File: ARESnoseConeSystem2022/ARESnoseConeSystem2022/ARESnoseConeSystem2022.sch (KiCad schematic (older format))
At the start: 15 parts, among them J1 436500200, J2 436500200, J3 BMP390_Headers, J4 ICM20948_Headers, J5 GPS_Headers1, J6 Transmitter_Headers1, J7 Conn_01x08, J8 Transmitter_Headers2, U1 BA05CC0WFP-E2, U2 Teensy4.1

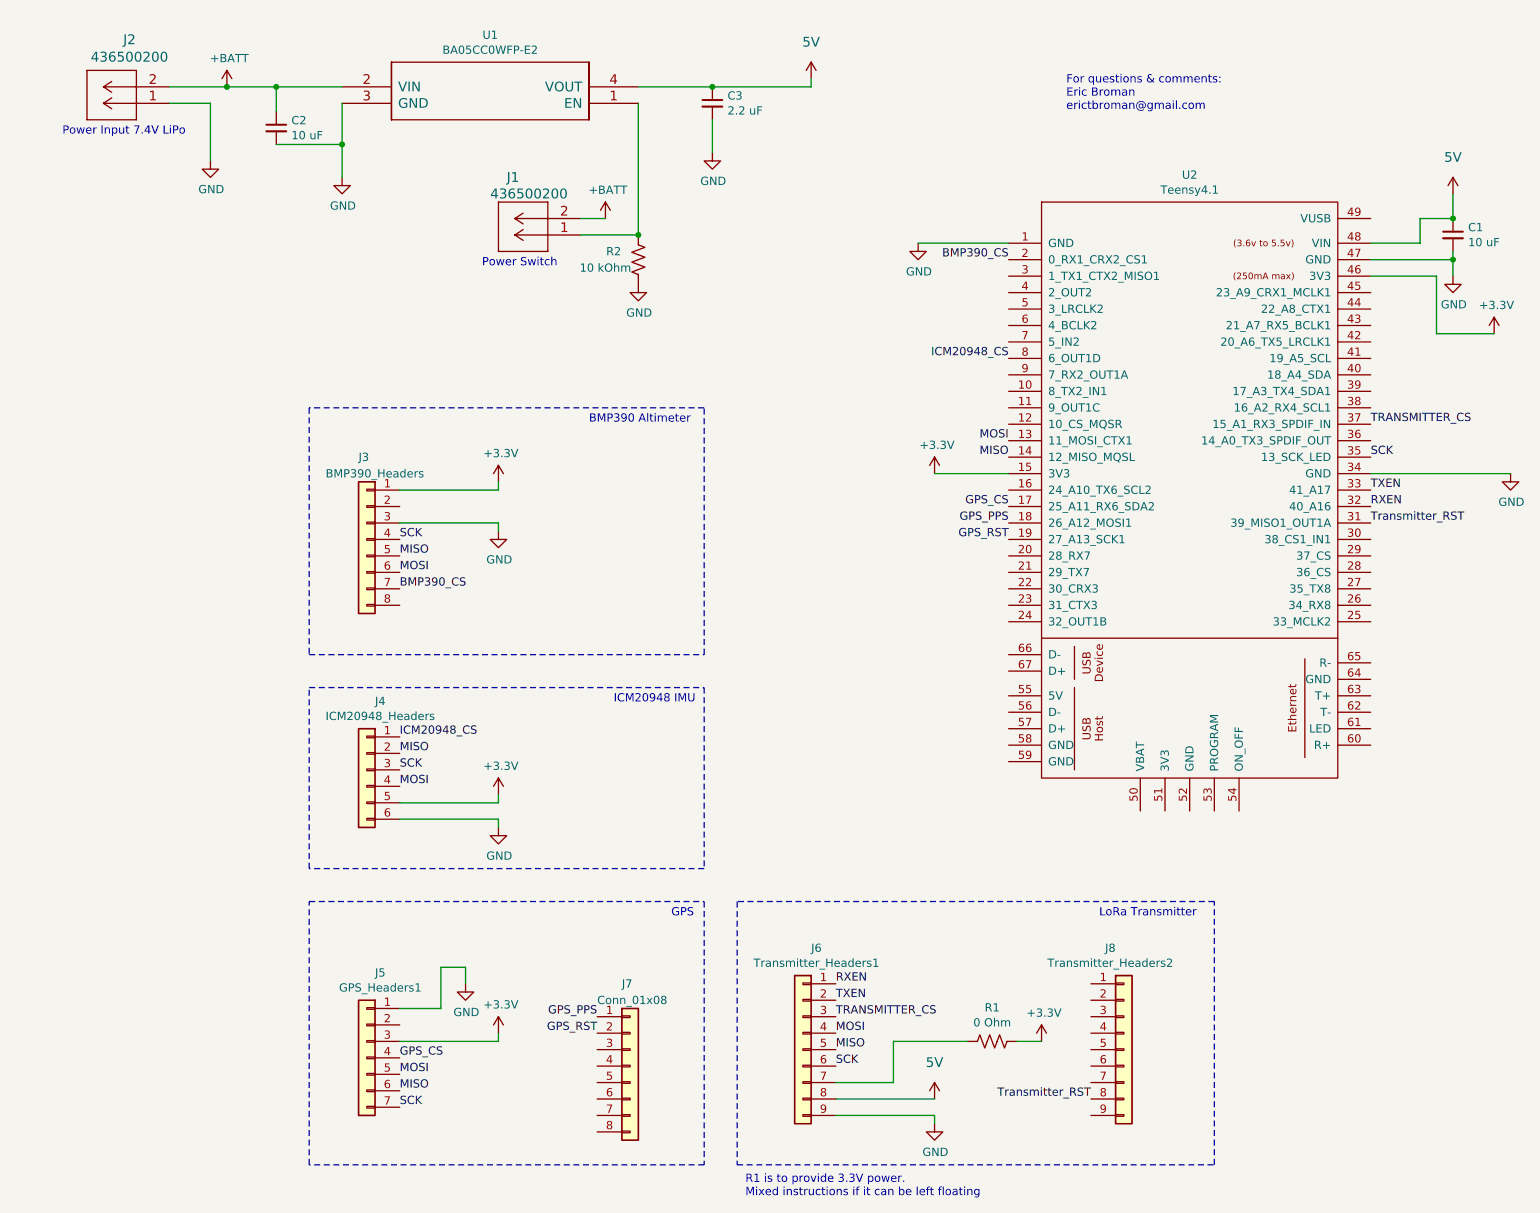
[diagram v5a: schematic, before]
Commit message: Finalized System V3
Added better radio board access and system power stabiity
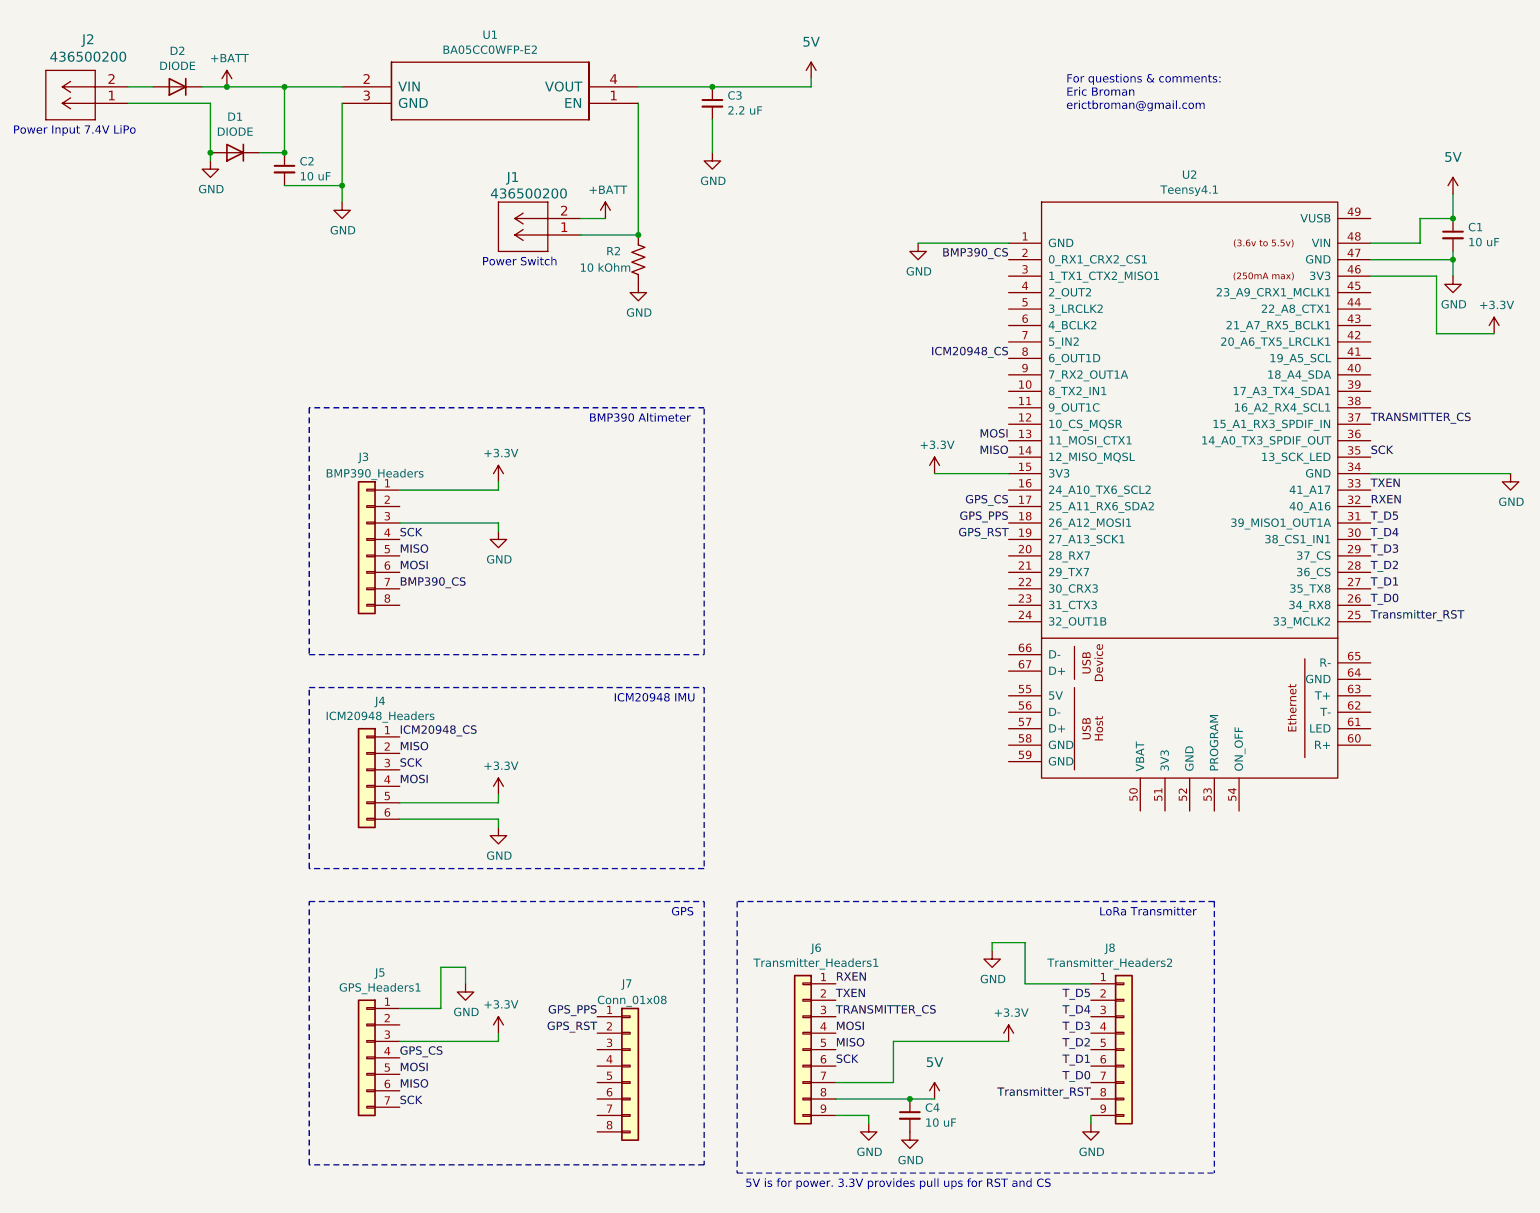
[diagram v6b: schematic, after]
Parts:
- removed R1: 0 Ohm, Resistor_SMD:R_0805_2012Metric_Pad1.15x1.40mm_HandSolder, symbol Device:R_US
- added C4: 10 uF, Capacitor_SMD:C_0805_2012Metric, symbol Device:C_Small
- added D1, D2: DIODE, Diode_SMD:D_0805_2012Metric, symbol Simulation_SPICE:DIODE
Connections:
- net +3V3: now also J6.7 (Pin_7)
- net +BATT: now also D1.2 (K), D2.2 (K); no longer J2.2
- net GND: now also J8.1 (Pin_1), J8.9 (Pin_9), C4.2, D1.1 (A)
- net Transmitter_RST: now also U2.25 (33_MCLK2); no longer U2.31 (39_MISO1_OUT1A)
- net T_D0: now reaches U2.26 (34_RX8)
- net T_D0: now also J8.7 (Pin_7)
- net T_D1: now reaches U2.27 (35_TX8)
- net T_D1: now also J8.6 (Pin_6)
- net T_D2: now reaches U2.28 (36_CS)
- net T_D2: now also J8.5 (Pin_5)
- net T_D3: now reaches U2.29 (37_CS)
- net T_D3: now also J8.4 (Pin_4)
- net T_D4: now reaches U2.30 (38_CS1_IN1)
- net T_D4: now also J8.3 (Pin_3)
- net at J6.8 (Pin_8): now also C4.1
- net T_D5: now reaches J8.2 (Pin_2)
- net T_D5: now also U2.31 (39_MISO1_OUT1A)
- new net: D2.1 (A), J2.2
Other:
- note added: "5V is for power. 3.3V provides pull ups for RST and CS"
- note removed: "R1 is to provide 3.3V power.\nMixed instructions if it can be left floating"
- moved on the sheet: C2, J2
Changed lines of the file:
@@
 L Device:C_Small C2
 U 1 1 617A460B
-P 1750 1100
-F 0 "C2" H 1842 1146 50  0000 L CNN
-F 1 "10 uF" H 1842 1055 50  0000 L CNN
-F 2 "Capacitor_SMD:C_0805_2012Metric_Pad1.15x1.40mm_HandSolder" H 1750 1100 50  0001 C CNN
-F 3 "~" H 1750 1100 50  0001 C CNN
-	1    1750 1100
+P 1800 1350
+F 0 "C2" H 1892 1396 50  0000 L CNN
+F 1 "10 uF" H 1892 1305 50  0000 L CNN
+F 2 "Capacitor_SMD:C_0805_2012Metric_Pad1.15x1.40mm_HandSolder" H 1800 1350 50  0001 C CNN
+F 3 "~" H 1800 1350 50  0001 C CNN
+	1    1800 1350
 	1    0    0    -1
 $EndComp
@@
 L power:GND #PWR0101
 U 1 1 6183E6B9
-P 2150 1400
-F 0 "#PWR0101" H 2150 1150 50  0001 C CNN
-F 1 "GND" H 2155 1227 50  0000 C CNN
-F 2 "" H 2150 1400 50  0001 C CNN
-F 3 "" H 2150 1400 50  0001 C CNN
-	1    2150 1400
+P 2150 1550
+F 0 "#PWR0101" H 2150 1300 50  0001 C CNN
+F 1 "GND" H 2155 1377 50  0000 C CNN
+F 2 "" H 2150 1550 50  0001 C CNN
+F 3 "" H 2150 1550 50  0001 C CNN
+	1    2150 1550
 	1    0    0    -1
 $EndComp
@@
 L power:GND #PWR0107
 U 1 1 61867FAF
-P 5750 7150
-F 0 "#PWR0107" H 5750 6900 50  0001 C CNN
-F 1 "GND" H 5755 6977 50  0000 C CNN
-F 2 "" H 5750 7150 50  0001 C CNN
-F 3 "" H 5750 7150 50  0001 C CNN
-	1    5750 7150
-	1    0    0    -1
-$EndComp
-Wire Wire Line
-	5750 7100 5750 7150
-Wire Wire Line
-	5150 7100 5750 7100
+P 5350 7150
+F 0 "#PWR0107" H 5350 6900 50  0001 C CNN
+F 1 "GND" H 5355 6977 50  0000 C CNN
+F 2 "" H 5350 7150 50  0001 C CNN
+F 3 "" H 5350 7150 50  0001 C CNN
+	1    5350 7150
+	1    0    0    -1
+$EndComp
+Wire Wire Line
+	5350 7100 5350 7150
 $Comp
 L ARESnoseConeSystem2022-rescue:5V-ARESnoseConeSystem2022-eagle-import #SUPPLY0103
@@
 $EndComp
 Wire Wire Line
-	5150 7000 5750 7000
-$Comp
-L Device:R_US R1
-U 1 1 61878C58
-P 6100 6650
-F 0 "R1" V 5895 6650 50  0000 C CNN
-F 1 "0 Ohm" V 5986 6650 50  0000 C CNN
-F 2 "Resistor_SMD:R_0805_2012Metric_Pad1.15x1.40mm_HandSolder" V 6140 6640 50  0001 C CNN
-F 3 "~" H 6100 6650 50  0001 C CNN
-	1    6100 6650
-	0    1    1    0
-$EndComp
-Wire Wire Line
-	6400 6650 6250 6650
-Wire Wire Line
-	5950 6650 5500 6650
-Wire Wire Line
 	5500 6650 5500 6900
 Wire Wire Line
@@
 Text Label 6700 7000 2    50   ~ 0
 Transmitter_RST
-Text Label 8400 3500 0    50   ~ 0
+Text Label 8400 4100 0    50   ~ 0
 Transmitter_RST
 Text Label 6200 3500 2    50   ~ 0
@@
 L power:+3.3V #PWR01
 U 1 1 618979DC
-P 6400 6650
-F 0 "#PWR01" H 6400 6500 50  0001 C CNN
-F 1 "+3.3V" H 6415 6823 50  0000 C CNN
-F 2 "" H 6400 6650 50  0001 C CNN
-F 3 "" H 6400 6650 50  0001 C CNN
-	1    6400 6650
+P 6200 6650
+F 0 "#PWR01" H 6200 6500 50  0001 C CNN
+F 1 "+3.3V" H 6215 6823 50  0000 C CNN
+F 2 "" H 6200 6650 50  0001 C CNN
+F 3 "" H 6200 6650 50  0001 C CNN
+	1    6200 6650
 	1    0    0    -1
 $EndComp
@@
 	1950 7400 1950 5800
 Wire Notes Line
-	4550 5800 4550 7400
-Wire Notes Line
-	4550 7400 7450 7400
-Wire Notes Line
-	7450 7400 7450 5800
+	4550 7450 7450 7450
 Wire Notes Line
 	7450 5800 4550 5800
@@
 Text Notes 6750 5900 0    50   ~ 0
 LoRa Transmitter
-Text Notes 4600 7600 0    50   ~ 0
-R1 is to provide 3.3V power.\nMixed instructions if it can be left floating
-Wire Wire Line
-	1750 850  1750 1000
-Connection ~ 1750 850
-Wire Wire Line
-	1750 850  2150 850
-Wire Wire Line
-	1750 1200 2150 1200
-Wire Wire Line
-	2150 1200 2150 1400
-Wire Wire Line
-	2150 1200 2150 950
-Connection ~ 2150 1200
+Text Notes 4600 7550 0    50   ~ 0
+5V is for power. 3.3V provides pull ups for RST and CS
 Wire Wire Line
 	5000 850  5000 800
@@
 	1    0    0    -1
 $EndComp
-Wire Wire Line
-	1450 850  1750 850
 $Comp
 L power:+BATT #PWR04
@@
 	1    0    0    -1
 $EndComp
-Wire Wire Line
-	1100 850  1450 850
-Connection ~ 1450 850
 Connection ~ 3950 1750
 Text Notes 6550 1000 0    50   ~ 0
@@
 L 2021-10-26_01-52-08:436500200 J2
 U 1 1 6179FE90
-P 1100 950
-F 0 "J2" H 1342 563 60  0000 C CNN
-F 1 "436500200" H 1342 669 60  0000 C CNN
-F 2 "Connector_Molex:Molex_Micro-Fit_3.0_43650-0200_1x02_P3.00mm_Horizontal" H 1500 890 60  0001 C CNN
-F 3 "" H 1100 950 60  0000 C CNN
-	1    1100 950
+P 850 950
+F 0 "J2" H 1092 563 60  0000 C CNN
+F 1 "436500200" H 1092 669 60  0000 C CNN
+F 2 "Connector_Molex:Molex_Micro-Fit_3.0_43650-0200_1x02_P3.00mm_Horizontal" H 1250 890 60  0001 C CNN
+F 3 "" H 850 950 60  0000 C CNN
+	1    850  950
 	-1   0    0    1
 $EndComp
@@
 $EndComp
 Wire Wire Line
-	1100 950  1350 950
-Wire Wire Line
-	1350 950  1350 1300
-Text Notes 450  1150 0    50   ~ 0
+	1350 950  1350 1250
+Text Notes 150  1150 0    50   ~ 0
 Power Input 7.4V LiPo
 $Comp
@@
 Wire Wire Line
 	3950 950  3950 1750
+$Comp
+L power:GND #PWR0111
+U 1 1 6202FF50
+P 6700 7150
+F 0 "#PWR0111" H 6700 6900 50  0001 C CNN
+F 1 "GND" H 6705 6977 50  0000 C CNN
+F 2 "" H 6700 7150 50  0001 C CNN
+F 3 "" H 6700 7150 50  0001 C CNN
+	1    6700 7150
+	1    0    0    -1
+$EndComp
+Wire Wire Line
+	6700 7100 6700 7150
+$Comp
+L power:GND #PWR0112
+U 1 1 62031060
+P 6100 6100
+F 0 "#PWR0112" H 6100 5850 50  0001 C CNN
+F 1 "GND" H 6105 5927 50  0000 C CNN
+F 2 "" H 6100 6100 50  0001 C CNN
+F 3 "" H 6100 6100 50  0001 C CNN
+	1    6100 6100
+	1    0    0    -1
+$EndComp
+Wire Wire Line
+	6100 6050 6100 6100
+Wire Wire Line
+	6700 6300 6300 6300
+Wire Wire Line
+	6300 6300 6300 6050
+Wire Wire Line
+	6300 6050 6100 6050
+Text Label 6700 6900 2    50   ~ 0
+T_D0
+Text Label 6700 6800 2    50   ~ 0
+T_D1
+Text Label 6700 6700 2    50   ~ 0
+T_D2
+Text Label 6700 6600 2    50   ~ 0
+T_D3
+Text Label 6700 6500 2    50   ~ 0
+T_D4
+Text Label 6700 6400 2    50   ~ 0
+T_D5
+Text Label 8400 4000 0    50   ~ 0
+T_D0
+Text Label 8400 3900 0    50   ~ 0
+T_D1
+Text Label 8400 3800 0    50   ~ 0
+T_D2
+Text Label 8400 3700 0    50   ~ 0
+T_D3
+Text Label 8400 3600 0    50   ~ 0
+T_D4
+Text Label 8400 3500 0    50   ~ 0
+T_D5
+Wire Wire Line
+	5350 7100 5150 7100
+$Comp
+L Device:C_Small C4
+U 1 1 62073826
+P 5600 7100
+F 0 "C4" H 5692 7146 50  0000 L CNN
+F 1 "10 uF" H 5692 7055 50  0000 L CNN
+F 2 "Capacitor_SMD:C_0805_2012Metric" H 5600 7100 50  0001 C CNN
+F 3 "~" H 5600 7100 50  0001 C CNN
+	1    5600 7100
+	1    0    0    -1
+$EndComp
+$Comp
+L power:GND #PWR010
+U 1 1 62074974
+P 5600 7200
+F 0 "#PWR010" H 5600 6950 50  0001 C CNN
+F 1 "GND" H 5605 7027 50  0000 C CNN
+F 2 "" H 5600 7200 50  0001 C CNN
+F 3 "" H 5600 7200 50  0001 C CNN
+	1    5600 7200
+	1    0    0    -1
+$EndComp
+Wire Wire Line
+	5500 6650 6200 6650
+Wire Notes Line
+	4550 5800 4550 7450
+Wire Notes Line
+	7450 5800 7450 7450
+Wire Wire Line
+	5150 7000 5600 7000
+Connection ~ 5600 7000
+Wire Wire Line
+	5600 7000 5750 7000
+$Comp
+L Simulation_SPICE:DIODE D1
+U 1 1 620A0FB6
+P 1500 1250
+F 0 "D1" H 1500 1467 50  0000 C CNN
+F 1 "DIODE" H 1500 1376 50  0000 C CNN
+F 2 "Diode_SMD:D_0805_2012Metric" H 1500 1250 50  0001 C CNN
+F 3 "~" H 1500 1250 50  0001 C CNN
+F 4 "Y" H 1500 1250 50  0001 L CNN "Spice_Netlist_Enabled"
+F 5 "D" H 1500 1250 50  0001 L CNN "Spice_Primitive"
+	1    1500 1250
+	1    0    0    -1
+$EndComp
+Connection ~ 1350 1250
+Wire Wire Line
+	1350 1250 1350 1300
+Wire Wire Line
+	1450 850  1800 850
+Wire Wire Line
+	1800 1450 2150 1450
+Wire Wire Line
+	2150 950  2150 1450
+Wire Wire Line
+	2150 1550 2150 1450
+Connection ~ 2150 1450
+Wire Wire Line
+	1650 1250 1800 1250
+Wire Wire Line
+	1800 1250 1800 850
+Connection ~ 1800 1250
+Connection ~ 1800 850
+Wire Wire Line
+	1800 850  2150 850
+$Comp
+L Simulation_SPICE:DIODE D2
+U 1 1 620B49DB
+P 1150 850
+F 0 "D2" H 1150 1067 50  0000 C CNN
+F 1 "DIODE" H 1150 976 50  0000 C CNN
+F 2 "Diode_SMD:D_0805_2012Metric" H 1150 850 50  0001 C CNN
+F 3 "~" H 1150 850 50  0001 C CNN
+F 4 "Y" H 1150 850 50  0001 L CNN "Spice_Netlist_Enabled"
+F 5 "D" H 1150 850 50  0001 L CNN "Spice_Primitive"
+	1    1150 850
+	1    0    0    -1
+$EndComp
+Wire Wire Line
+	850  850  1000 850
+Wire Wire Line
+	1300 850  1450 850
+Connection ~ 1450 850
+Wire Wire Line
+	850  950  1350 950
 $EndSCHEMATC
